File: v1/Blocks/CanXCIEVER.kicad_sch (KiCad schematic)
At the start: 2 parts, among them IC45 TCAN337DCNR, J5 TC0203620000G

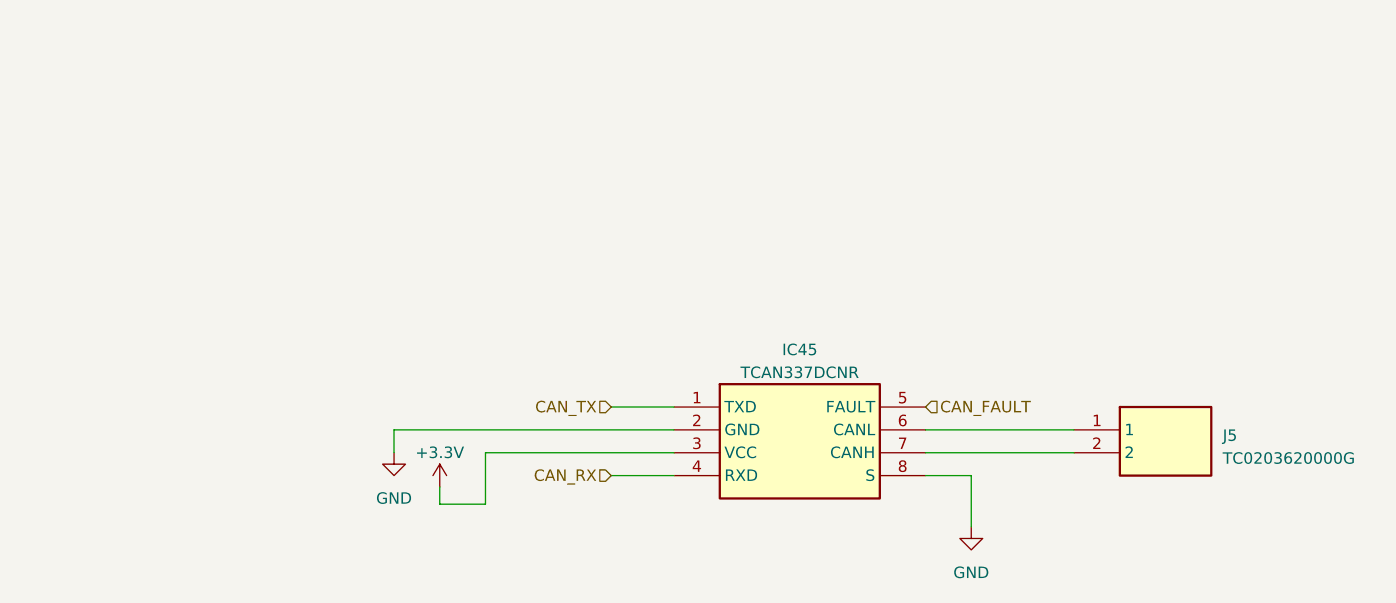
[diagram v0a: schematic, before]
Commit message: Update views, to make drawing sheets smaller where necessary
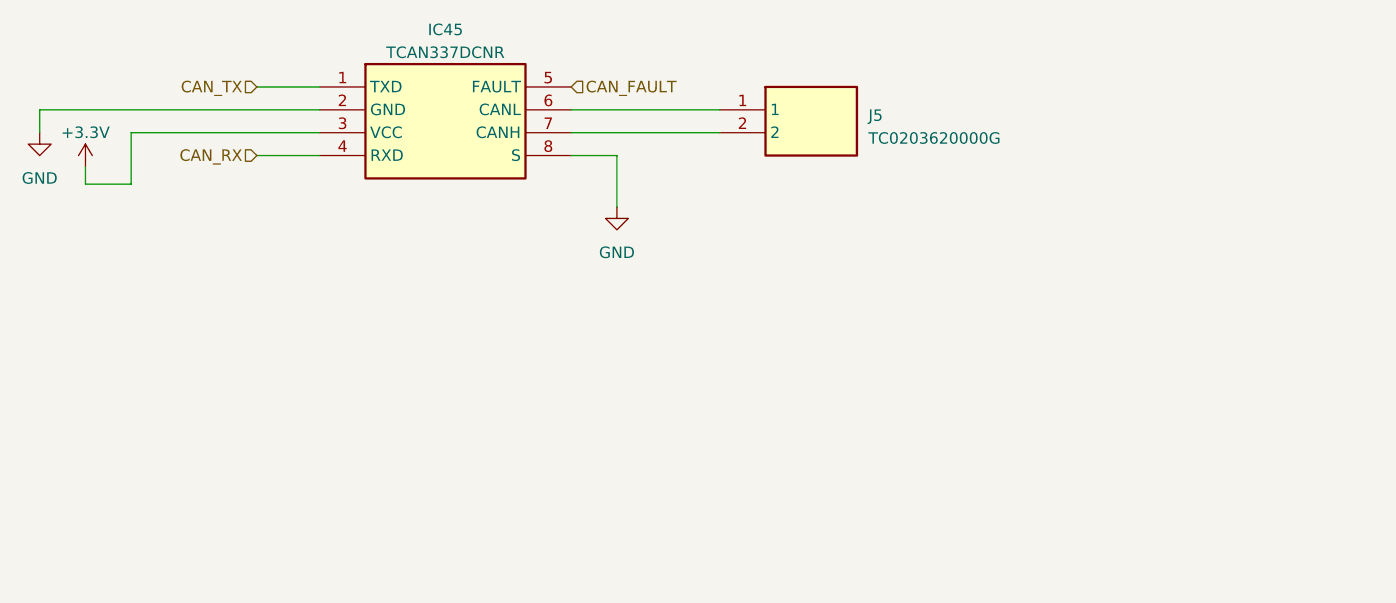
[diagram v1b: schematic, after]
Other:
- moved on the sheet: IC45, J5
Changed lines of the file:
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@@
 (kicad_sch (version 20230121) (generator eeschema)
-  (paper "A4")
-  (wire (pts (xy 103.505 104.14) (xy 124.46 104.14))
+  (paper "A5")
+  (wire (pts (xy 64.135 68.58) (xy 85.09 68.58))
     (stroke (width 0) (type default))
   )
-  (wire (pts (xy 98.425 109.855) (xy 103.505 109.855))
+  (wire (pts (xy 59.055 74.295) (xy 64.135 74.295))
     (stroke (width 0) (type default))
   )
-  (wire (pts (xy 152.4 104.14) (xy 168.91 104.14))
+  (wire (pts (xy 113.03 68.58) (xy 129.54 68.58))
     (stroke (width 0) (type default))
   )
-  (wire (pts (xy 157.48 106.68) (xy 157.48 112.395))
+  (wire (pts (xy 118.11 71.12) (xy 118.11 76.835))
     (stroke (width 0) (type default))
   )
-  (wire (pts (xy 93.345 104.14) (xy 93.345 101.6))
+  (wire (pts (xy 53.975 68.58) (xy 53.975 66.04))
     (stroke (width 0) (type default))
   )
-  (wire (pts (xy 93.345 101.6) (xy 124.46 101.6))
+  (wire (pts (xy 53.975 66.04) (xy 85.09 66.04))
     (stroke (width 0) (type default))
   )
-  (wire (pts (xy 152.4 101.6) (xy 168.91 101.6))
+  (wire (pts (xy 113.03 66.04) (xy 129.54 66.04))
     (stroke (width 0) (type default))
   )
-  (wire (pts (xy 98.425 107.95) (xy 98.425 109.855))
+  (wire (pts (xy 59.055 72.39) (xy 59.055 74.295))
     (stroke (width 0) (type default))
   )
-  (wire (pts (xy 152.4 106.68) (xy 157.48 106.68))
+  (wire (pts (xy 113.03 71.12) (xy 118.11 71.12))
     (stroke (width 0) (type default))
   )
-  (wire (pts (xy 117.475 106.68) (xy 124.46 106.68))
+  (wire (pts (xy 78.105 71.12) (xy 85.09 71.12))
     (stroke (width 0) (type default))
   )
-  (wire (pts (xy 103.505 109.855) (xy 103.505 104.14))
+  (wire (pts (xy 64.135 74.295) (xy 64.135 68.58))
     (stroke (width 0) (type default))
   )
-  (wire (pts (xy 117.475 99.06) (xy 124.46 99.06))
+  (wire (pts (xy 78.105 63.5) (xy 85.09 63.5))
     (stroke (width 0) (type default))
   )
-  (hierarchical_label "CAN_FAULT" (shape input) (at 152.4 99.06 0) (fields_autoplaced)
+  (hierarchical_label "CAN_FAULT" (shape input) (at 113.03 63.5 0) (fields_autoplaced)
     (effects (font (size 1.27 1.27)) (justify left))
   )
-  (hierarchical_label "CAN_TX" (shape input) (at 117.475 99.06 180) (fields_autoplaced)
+  (hierarchical_label "CAN_TX" (shape input) (at 78.105 63.5 180) (fields_autoplaced)
     (effects (font (size 1.27 1.27)) (justify right))
   )
-  (hierarchical_label "CAN_RX" (shape input) (at 117.475 106.68 180) (fields_autoplaced)
+  (hierarchical_label "CAN_RX" (shape input) (at 78.105 71.12 180) (fields_autoplaced)
     (effects (font (size 1.27 1.27)) (justify right))
   )
-  (symbol (lib_id "power:+3.3V") (at 98.425 107.95 0) (unit 1)
+  (symbol (lib_id "power:+3.3V") (at 59.055 72.39 0) (unit 1)
     (in_bom yes) (on_board yes) (dnp no) (fields_autoplaced)
-    (property "Reference" "#PWR0117" (at 98.425 111.76 0)
+    (property "Reference" "#PWR0117" (at 59.055 76.2 0)
       (effects (font (size 1.27 1.27)) hide)
     )
-    (property "Value" "+3.3V" (at 98.425 104.14 0)
+    (property "Value" "+3.3V" (at 59.055 68.58 0)
       (effects (font (size 1.27 1.27)))
     )
-    (property "Footprint" "" (at 98.425 107.95 0)
+    (property "Footprint" "" (at 59.055 72.39 0)
       (effects (font (size 1.27 1.27)) hide)
     )
-    (property "Datasheet" "" (at 98.425 107.95 0)
+    (property "Datasheet" "" (at 59.055 72.39 0)
       (effects (font (size 1.27 1.27)) hide)
     )
@@
     )
   )
-  (symbol (lib_id "power:GND") (at 157.48 112.395 0) (unit 1)
+  (symbol (lib_id "power:GND") (at 118.11 76.835 0) (unit 1)
     (in_bom yes) (on_board yes) (dnp no) (fields_autoplaced)
-    (property "Reference" "#PWR0124" (at 157.48 118.745 0)
+    (property "Reference" "#PWR0124" (at 118.11 83.185 0)
       (effects (font (size 1.27 1.27)) hide)
     )
-    (property "Value" "GND" (at 157.48 117.475 0)
+    (property "Value" "GND" (at 118.11 81.915 0)
       (effects (font (size 1.27 1.27)))
     )
-    (property "Footprint" "" (at 157.48 112.395 0)
+    (property "Footprint" "" (at 118.11 76.835 0)
       (effects (font (size 1.27 1.27)) hide)
     )
-    (property "Datasheet" "" (at 157.48 112.395 0)
+    (property "Datasheet" "" (at 118.11 76.835 0)
       (effects (font (size 1.27 1.27)) hide)
     )
@@
     )
   )
-  (symbol (lib_id "TCAN337DCNR:TCAN337DCNR") (at 124.46 99.06 0) (unit 1)
+  (symbol (lib_id "TCAN337DCNR:TCAN337DCNR") (at 85.09 63.5 0) (unit 1)
     (in_bom yes) (on_board yes) (dnp no) (fields_autoplaced)
-    (property "Reference" "IC45" (at 138.43 92.71 0)
+    (property "Reference" "IC45" (at 99.06 57.15 0)
       (effects (font (size 1.27 1.27)))
     )
-    (property "Value" "TCAN337DCNR" (at 138.43 95.25 0)
+    (property "Value" "TCAN337DCNR" (at 99.06 59.69 0)
       (effects (font (size 1.27 1.27)))
     )
-    (property "Footprint" "TCAN337DCNR:SOT65P280X145-8N" (at 148.59 193.98 0)
+    (property "Footprint" "TCAN337DCNR:SOT65P280X145-8N" (at 109.22 158.42 0)
       (effects (font (size 1.27 1.27)) (justify left top) hide)
     )
-    (property "Datasheet" "https://www.ti.com/lit/gpn/TCAN337" (at 148.59 293.98 0)
+    (property "Datasheet" "https://www.ti.com/lit/gpn/TCAN337" (at 109.22 258.42 0)
       (effects (font (size 1.27 1.27)) (justify left top) hide)
     )
-    (property "Height" "1.45" (at 148.59 493.98 0)
+    (property "Height" "1.45" (at 109.22 458.42 0)
       (effects (font (size 1.27 1.27)) (justify left top) hide)
     )
-    (property "Mouser Part Number" "595-TCAN337DCNR" (at 148.59 593.98 0)
+    (property "Mouser Part Number" "595-TCAN337DCNR" (at 109.22 558.42 0)
       (effects (font (size 1.27 1.27)) (justify left top) hide)
     )
-    (property "Mouser Price/Stock" "https://www.mouser.co.uk/ProductDetail/Texas-Instruments/TCAN337DCNR?qs=gMfM3zrbS4r1ZrvbjcW09A%3D%3D" (at 148.59 693.98 0)
+    (property "Mouser Price/Stock" "https://www.mouser.co.uk/ProductDetail/Texas-Instruments/TCAN337DCNR?qs=gMfM3zrbS4r1ZrvbjcW09A%3D%3D" (at 109.22 658.42 0)
       (effects (font (size 1.27 1.27)) (justify left top) hide)
     )
-    (property "Manufacturer_Name" "Texas Instruments" (at 148.59 793.98 0)
+    (property "Manufacturer_Name" "Texas Instruments" (at 109.22 758.42 0)
       (effects (font (size 1.27 1.27)) (justify left top) hide)
     )
-    (property "Manufacturer_Part_Number" "TCAN337DCNR" (at 148.59 893.98 0)
+    (property "Manufacturer_Part_Number" "TCAN337DCNR" (at 109.22 858.42 0)
       (effects (font (size 1.27 1.27)) (justify left top) hide)
     )
@@
     )
   )
-  (symbol (lib_id "TC0203620000G:TC0203620000G") (at 168.91 101.6 0) (unit 1)
+  (symbol (lib_id "TC0203620000G:TC0203620000G") (at 129.54 66.04 0) (unit 1)
     (in_bom yes) (on_board yes) (dnp no) (fields_autoplaced)
-    (property "Reference" "J5" (at 185.42 102.235 0)
+    (property "Reference" "J5" (at 146.05 66.675 0)
       (effects (font (size 1.27 1.27)) (justify left))
     )
-    (property "Value" "TC0203620000G" (at 185.42 104.775 0)
+    (property "Value" "TC0203620000G" (at 146.05 69.215 0)
       (effects (font (size 1.27 1.27)) (justify left))
     )
-    (property "Footprint" "TC0203620000G:TC0203620000G" (at 185.42 196.52 0)
+    (property "Footprint" "TC0203620000G:TC0203620000G" (at 146.05 160.96 0)
       (effects (font (size 1.27 1.27)) (justify left top) hide)
     )
-    (property "Datasheet" "https://componentsearchengine.com/Datasheets/1/TC0203620000G.pdf" (at 185.42 296.52 0)
+    (property "Datasheet" "https://componentsearchengine.com/Datasheets/1/TC0203620000G.pdf" (at 146.05 260.96 0)
       (effects (font (size 1.27 1.27)) (justify left top) hide)
     )
-    (property "Height" "10.5" (at 185.42 496.52 0)
+    (property "Height" "10.5" (at 146.05 460.96 0)
       (effects (font (size 1.27 1.27)) (justify left top) hide)
     )
-    (property "Mouser Part Number" "649-TC02036200J0G" (at 185.42 596.52 0)
+    (property "Mouser Part Number" "649-TC02036200J0G" (at 146.05 560.96 0)
       (effects (font (size 1.27 1.27)) (justify left top) hide)
     )
-    (property "Mouser Price/Stock" "https://www.mouser.co.uk/ProductDetail/Amphenol-Anytek/TC0203620000G?qs=Mv7BduZupUiHURQaUHJ1XQ%3D%3D" (at 185.42 696.52 0)
+    (property "Mouser Price/Stock" "https://www.mouser.co.uk/ProductDetail/Amphenol-Anytek/TC0203620000G?qs=Mv7BduZupUiHURQaUHJ1XQ%3D%3D" (at 146.05 660.96 0)
       (effects (font (size 1.27 1.27)) (justify left top) hide)
     )
-    (property "Manufacturer_Name" "Amphenol" (at 185.42 796.52 0)
+    (property "Manufacturer_Name" "Amphenol" (at 146.05 760.96 0)
       (effects (font (size 1.27 1.27)) (justify left top) hide)
     )
-    (property "Manufacturer_Part_Number" "TC0203620000G" (at 185.42 896.52 0)
+    (property "Manufacturer_Part_Number" "TC0203620000G" (at 146.05 860.96 0)
       (effects (font (size 1.27 1.27)) (justify left top) hide)
     )
@@
     )
   )
-  (symbol (lib_id "power:GND") (at 93.345 104.14 0) (unit 1)
+  (symbol (lib_id "power:GND") (at 53.975 68.58 0) (unit 1)
     (in_bom yes) (on_board yes) (dnp no) (fields_autoplaced)
-    (property "Reference" "#PWR0116" (at 93.345 110.49 0)
+    (property "Reference" "#PWR0116" (at 53.975 74.93 0)
       (effects (font (size 1.27 1.27)) hide)
     )
-    (property "Value" "GND" (at 93.345 109.22 0)
+    (property "Value" "GND" (at 53.975 73.66 0)
       (effects (font (size 1.27 1.27)))
     )
-    (property "Footprint" "" (at 93.345 104.14 0)
+    (property "Footprint" "" (at 53.975 68.58 0)
       (effects (font (size 1.27 1.27)) hide)
     )
-    (property "Datasheet" "" (at 93.345 104.14 0)
+    (property "Datasheet" "" (at 53.975 68.58 0)
       (effects (font (size 1.27 1.27)) hide)
     )
